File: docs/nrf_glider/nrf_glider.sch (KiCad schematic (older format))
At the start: 27 parts, among them J1 PROG, J2 Conn_01x12_Male, J3 UART, J4 Conn_01x12_Female, J5 Conn_01x12_Female, M1 Servo Left, M2 Servo Right, SW1 TRIM, SW2 SW_SPST, U1 MSP430G2553IPW20, U2 25LC640, U3 NRF24L01_Breakout, U4 LM1117-3.3, U5 LM1117-3.3

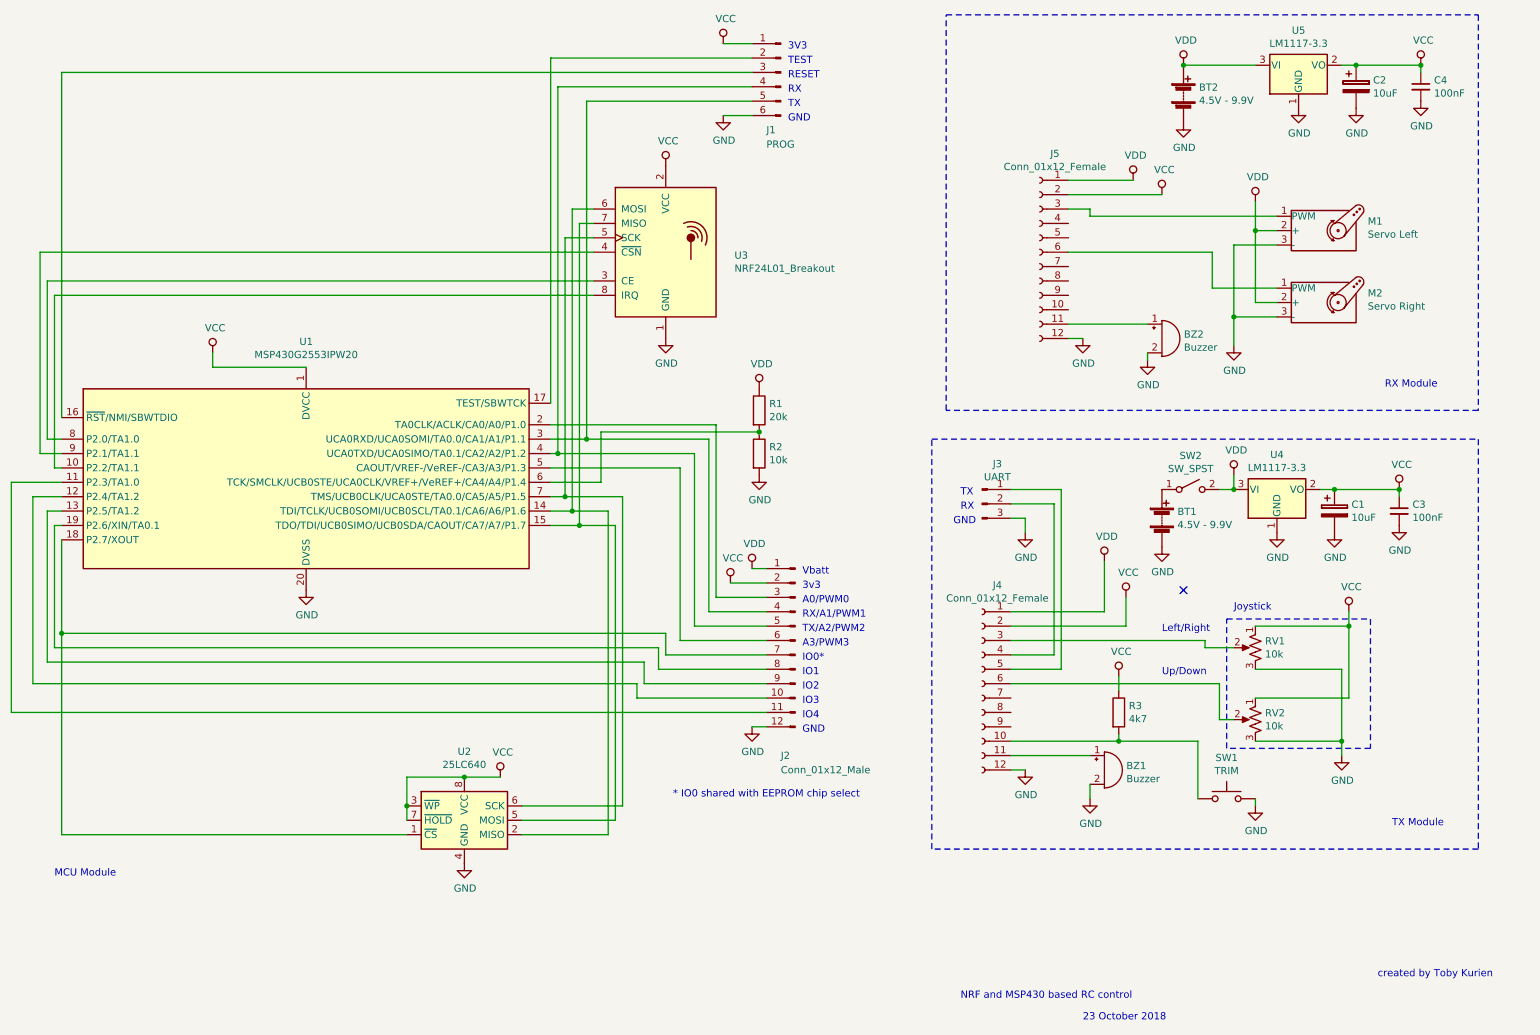
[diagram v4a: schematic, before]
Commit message: split up schematic into 3
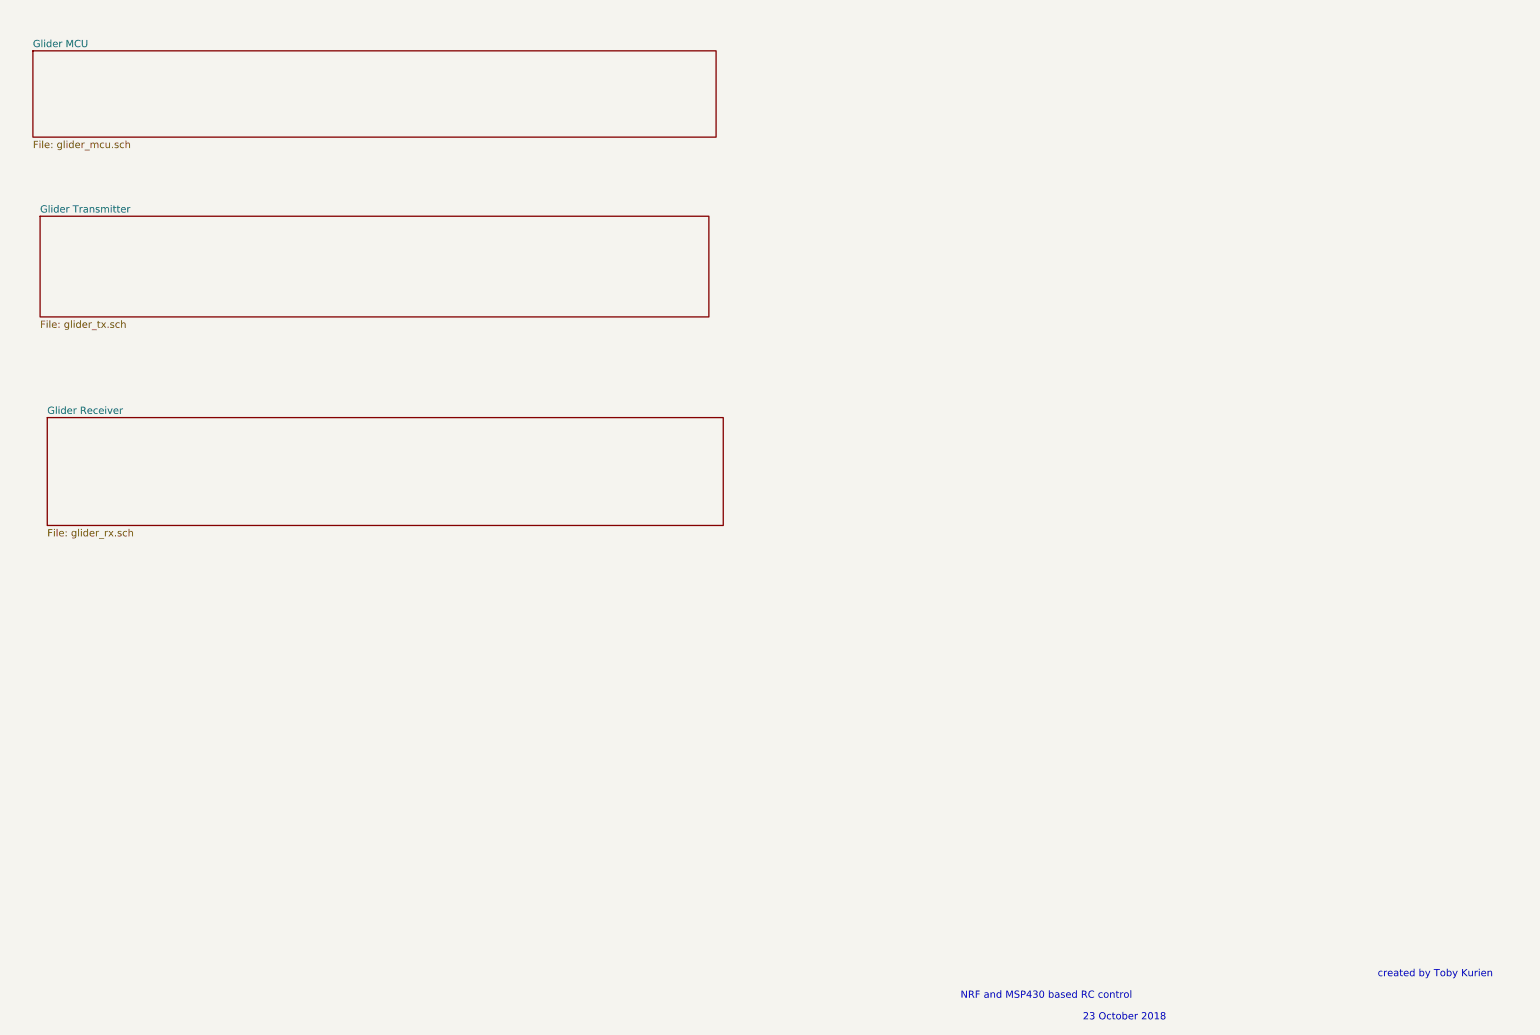
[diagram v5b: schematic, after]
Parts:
- removed BT1, BT2: 4.5V - 9.9V, Connector_PinHeader_2.54mm:PinHeader_1x02_P2.54mm_Vertical, symbol Device:Battery
- removed BZ1, BZ2: Buzzer, Buzzer_Beeper:Buzzer_15x7.5RM7.6, symbol Device:Buzzer
- removed C1, C2: 10uF, Capacitor_THT:CP_Radial_D8.0mm_P2.50mm, symbol Device:CP
- removed C3, C4: 100nF, Capacitor_THT:C_Disc_D5.0mm_W2.5mm_P5.00mm, symbol Device:C_Small
- removed J1: PROG, Connector_PinHeader_2.54mm:PinHeader_1x06_P2.54mm_Vertical, symbol Connector:Conn_01x06_Male
- removed J2: Conn_01x12_Male, Connector_PinHeader_2.54mm:PinHeader_1x12_P2.54mm_Vertical, symbol Connector:Conn_01x12_Male
- removed J3: UART, Connector_PinHeader_2.54mm:PinHeader_1x03_P2.54mm_Horizontal, symbol Connector:Conn_01x03_Male
- removed J4, J5: Conn_01x12_Female, Connector_PinHeader_2.54mm:PinHeader_1x12_P2.54mm_Vertical, symbol Connector:Conn_01x12_Female
- removed M1: Servo Left, Connector_PinHeader_2.54mm:PinHeader_1x03_P2.54mm_Vertical, symbol Motor:Motor_Servo
- removed M2: Servo Right, Connector_PinHeader_2.54mm:PinHeader_1x03_P2.54mm_Vertical, symbol Motor:Motor_Servo
- removed R1: 20k, Resistor_THT:R_Axial_DIN0411_L9.9mm_D3.6mm_P12.70mm_Horizontal, symbol Device:R
- removed R2: 10k, Resistor_THT:R_Axial_DIN0411_L9.9mm_D3.6mm_P12.70mm_Horizontal, symbol Device:R
- removed R3: 4k7, Resistor_THT:R_Axial_DIN0411_L9.9mm_D3.6mm_P12.70mm_Horizontal, symbol Device:R
- removed RV1, RV2: 10k, Potentiometer_THT:Potentiometer_ACP_CA9-V10_Vertical, symbol Device:R_POT_US
- removed SW1: TRIM, Button_Switch_THT:SW_PUSH_6mm_H5mm, symbol Switch:SW_Push
- removed SW2: SW_SPST, symbol Switch:SW_SPST
- removed U1: MSP430G2553IPW20, Package_DIP:DIP-20_W7.62mm, symbol MCU_Texas_MSP430:MSP430G2553IPW20
- removed U2: 25LC640, Package_DIP:DIP-8_W7.62mm, symbol Memory_EEPROM:25LCxxx
- removed U3: NRF24L01_Breakout, RF_Module:nRF24L01_Breakout, symbol RF:NRF24L01_Breakout
- removed U4, U5: LM1117-3.3, symbol Regulator_Linear:LM1117-3.3
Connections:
- no-connect marks 1 -> 0
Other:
- note removed: "* IO0 shared with EEPROM chip select"
- note removed: "3V3"
- note removed: "3v3"
- note removed: "A0/PWM0"
- note removed: "A3/PWM3"
- note removed: "GND"
- note removed: "IO0*"
- note removed: "IO1"
- note removed: "IO2"
- note removed: "IO3"
- note removed: "IO4"
- note removed: "Joystick"
- note removed: "Left/Right\n"
- note removed: "MCU Module"
- note removed: "RESET"
- note removed: "RX"
- note removed: "RX Module"
- note removed: "RX/A1/PWM1"
- note removed: "TEST"
- note removed: "TX"
- note removed: "TX Module"
- note removed: "TX/A2/PWM2"
- note removed: "Up/Down"
- note removed: "Vbatt\n"

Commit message: added hierarchical sheets and labels
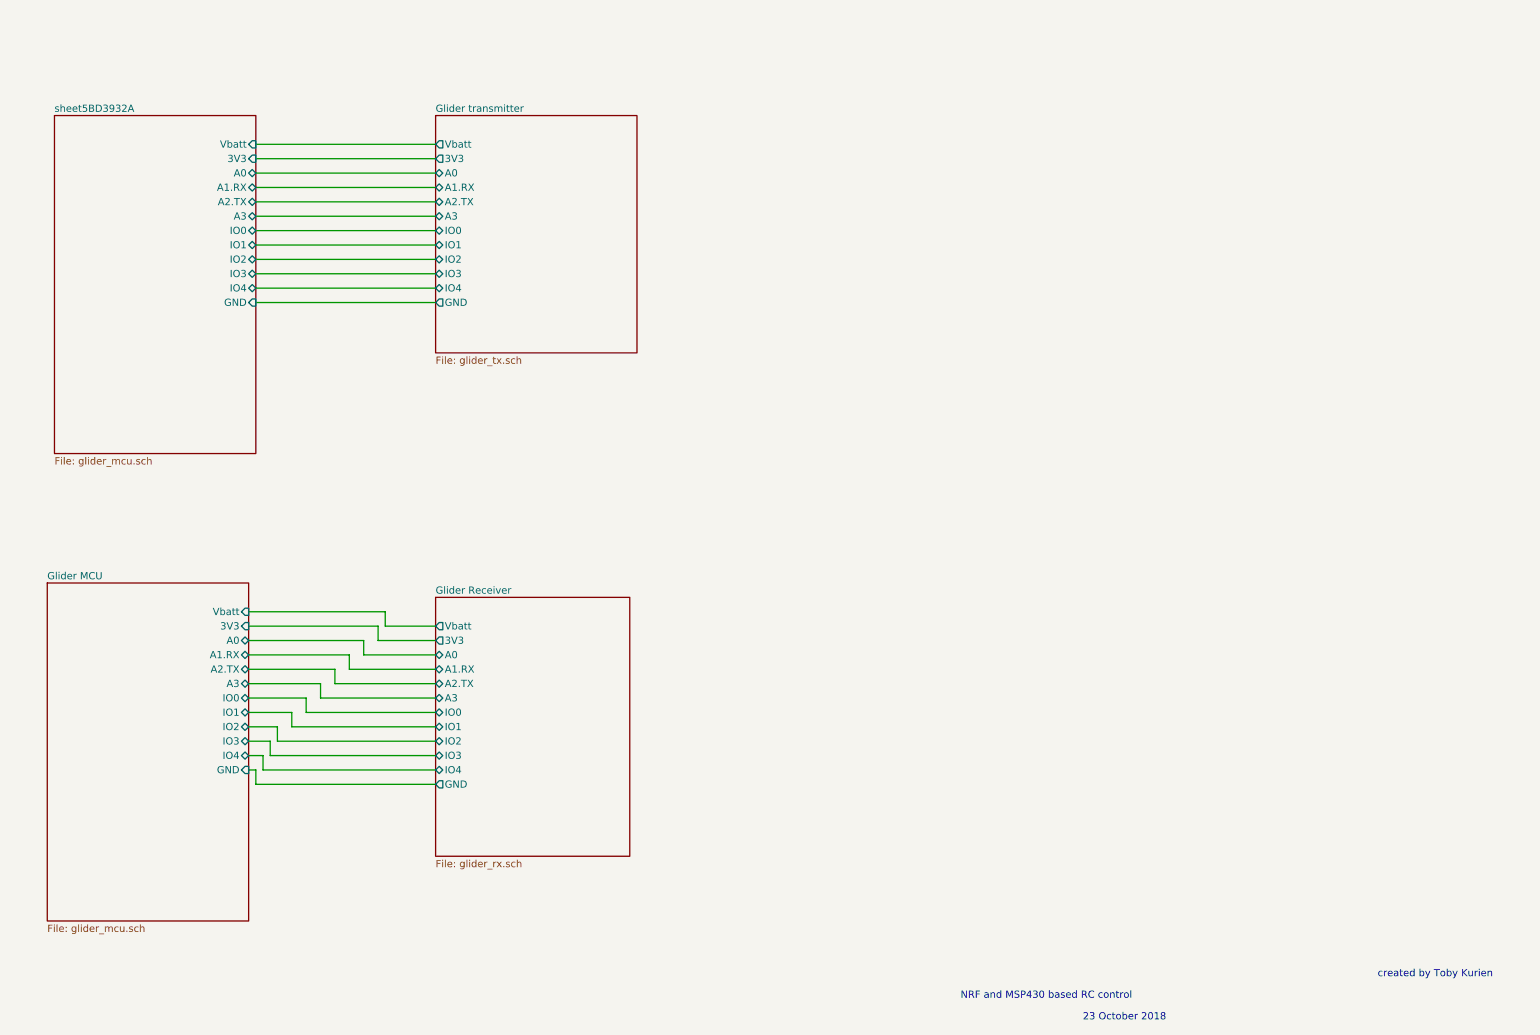
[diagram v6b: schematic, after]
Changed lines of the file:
@@
 $Descr A4 11693 8268
 encoding utf-8
-Sheet 1 4
+Sheet 1 5
 Title ""
 Date ""
@@
 created by Toby Kurien
 $Sheet
-S 950  900  4750 600
-U 5BD30486
+S 1050 4600 1400 2350
+U 5BD3906D
 F0 "Glider MCU" 50
 F1 "glider_mcu.sch" 50
+F2 "Vbatt" I R 2450 4800 50
+F3 "3V3" I R 2450 4900 50
+F4 "A0" B R 2450 5000 50
+F5 "A1.RX" B R 2450 5100 50
+F6 "A2.TX" B R 2450 5200 50
+F7 "A3" B R 2450 5300 50
+F8 "IO0" B R 2450 5400 50
+F9 "IO1" B R 2450 5500 50
+F10 "IO2" B R 2450 5600 50
+F11 "IO3" B R 2450 5700 50
+F12 "IO4" B R 2450 5800 50
+F13 "GND" I R 2450 5900 50
 $EndSheet
 $Sheet
-S 1000 2050 4650 700
-U 5BD30515
-F0 "Glider Transmitter" 50
+S 3750 1350 1400 1650
+U 5BD39174
+F0 "Glider transmitter" 50
 F1 "glider_tx.sch" 50
+F2 "Vbatt" O L 3750 1550 50
+F3 "3V3" O L 3750 1650 50
+F4 "A0" B L 3750 1750 50
+F5 "A1.RX" B L 3750 1850 50
+F6 "A2.TX" B L 3750 1950 50
+F7 "A3" B L 3750 2050 50
+F8 "IO0" B L 3750 2150 50
+F9 "IO1" B L 3750 2250 50
+F10 "IO2" B L 3750 2350 50
+F11 "IO3" B L 3750 2450 50
+F12 "IO4" B L 3750 2550 50
+F13 "GND" O L 3750 2650 50
 $EndSheet
 $Sheet
-S 1050 3450 4700 750
-U 5BD305D5
+S 3750 4700 1350 1800
+U 5BD39234
 F0 "Glider Receiver" 50
 F1 "glider_rx.sch" 50
+F2 "Vbatt" O L 3750 4900 50
+F3 "3V3" O L 3750 5000 50
+F4 "A0" B L 3750 5100 50
+F5 "A1.RX" B L 3750 5200 50
+F6 "A2.TX" B L 3750 5300 50
+F7 "A3" B L 3750 5400 50
+F8 "IO0" B L 3750 5500 50
+F9 "IO1" B L 3750 5600 50
+F10 "IO2" B L 3750 5700 50
+F11 "IO3" B L 3750 5800 50
+F12 "IO4" B L 3750 5900 50
+F13 "GND" O L 3750 6000 50
 $EndSheet
+$Sheet
+S 1100 1350 1400 2350
+U 5BD39338
+F0 "sheet5BD3932A" 50
+F1 "glider_mcu.sch" 50
+F2 "Vbatt" I R 2500 1550 50
+F3 "3V3" I R 2500 1650 50
+F4 "A0" B R 2500 1750 50
+F5 "A1.RX" B R 2500 1850 50
+F6 "A2.TX" B R 2500 1950 50
+F7 "A3" B R 2500 2050 50
+F8 "IO0" B R 2500 2150 50
+F9 "IO1" B R 2500 2250 50
+F10 "IO2" B R 2500 2350 50
+F11 "IO3" B R 2500 2450 50
+F12 "IO4" B R 2500 2550 50
+F13 "GND" I R 2500 2650 50
+$EndSheet
+Wire Wire Line
+	3750 4900 3400 4900
+Wire Wire Line
+	3400 4900 3400 4800
+Wire Wire Line
+	3400 4800 2450 4800
+Wire Wire Line
+	2450 4900 3350 4900
+Wire Wire Line
+	3350 4900 3350 5000
+Wire Wire Line
+	3350 5000 3750 5000
+Wire Wire Line
+	3750 5100 3250 5100
+Wire Wire Line
+	3250 5100 3250 5000
+Wire Wire Line
+	3250 5000 2450 5000
+Wire Wire Line
+	2450 5100 3150 5100
+Wire Wire Line
+	3150 5100 3150 5200
+Wire Wire Line
+	3150 5200 3750 5200
+Wire Wire Line
+	3750 5300 3050 5300
+Wire Wire Line
+	3050 5300 3050 5200
+Wire Wire Line
+	3050 5200 2450 5200
+Wire Wire Line
+	2450 5300 2950 5300
+Wire Wire Line
+	2950 5300 2950 5400
+Wire Wire Line
+	2950 5400 3750 5400
+Wire Wire Line
+	3750 5500 2850 5500
+Wire Wire Line
+	2850 5500 2850 5400
+Wire Wire Line
+	2850 5400 2450 5400
+Wire Wire Line
+	2450 5500 2750 5500
+Wire Wire Line
+	2750 5500 2750 5600
+Wire Wire Line
+	2750 5600 3750 5600
+Wire Wire Line
+	2450 5600 2650 5600
+Wire Wire Line
+	2650 5600 2650 5700
+Wire Wire Line
+	2650 5700 3750 5700
+Wire Wire Line
+	2450 5700 2600 5700
+Wire Wire Line
+	2600 5700 2600 5800
+Wire Wire Line
+	2600 5800 3750 5800
+Wire Wire Line
+	2450 5800 2550 5800
+Wire Wire Line
+	2550 5800 2550 5900
+Wire Wire Line
+	2550 5900 3750 5900
+Wire Wire Line
+	2450 5900 2500 5900
+Wire Wire Line
+	2500 5900 2500 6000
+Wire Wire Line
+	2500 6000 3750 6000
+Wire Wire Line
+	2500 1550 3750 1550
+Wire Wire Line
+	2500 1650 3750 1650
+Wire Wire Line
+	2500 1750 3750 1750
+Wire Wire Line
+	2500 1850 3750 1850
+Wire Wire Line
+	2500 1950 3750 1950
+Wire Wire Line
+	2500 2050 3750 2050
+Wire Wire Line
+	2500 2150 3750 2150
+Wire Wire Line
+	2500 2250 3750 2250
+Wire Wire Line
+	2500 2350 3750 2350
+Wire Wire Line
+	2500 2450 3750 2450
+Wire Wire Line
+	2500 2550 3750 2550
+Wire Wire Line
+	2500 2650 3750 2650
 $EndSCHEMATC
